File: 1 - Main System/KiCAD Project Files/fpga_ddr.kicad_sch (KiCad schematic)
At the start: 71 parts, among them IC8 IS43TR16640C-125JBL, IC9 IS43TR16640C-125JBL, U17 XC7Z020-1CLG484C

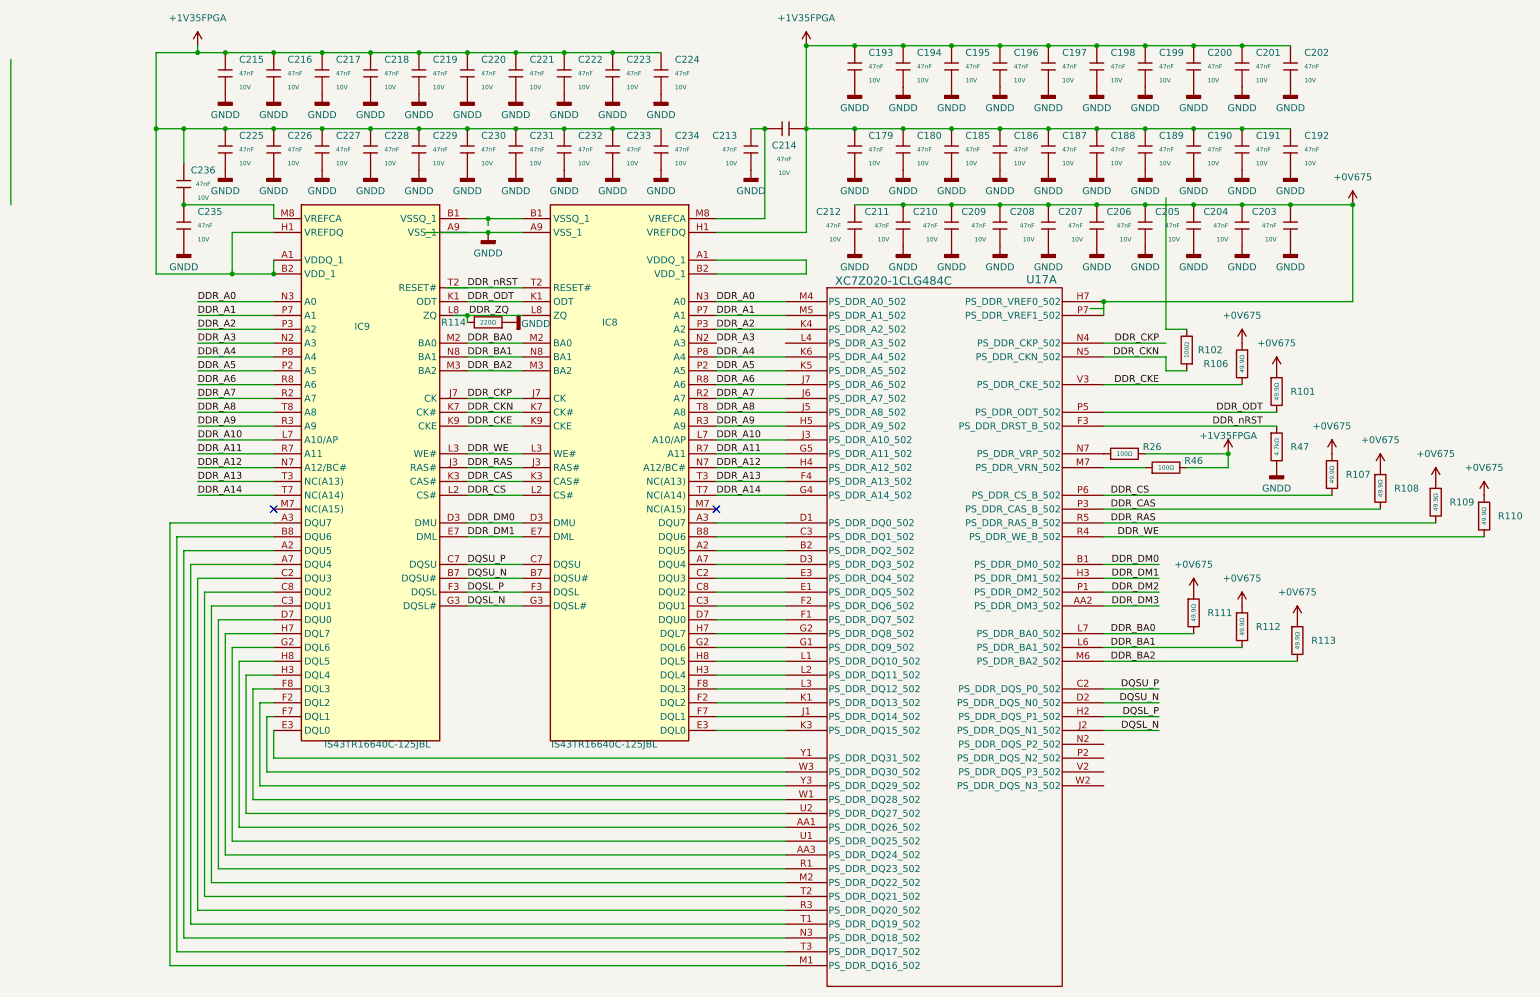
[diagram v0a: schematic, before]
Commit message: Routing DDR3 Completed (pre-review)
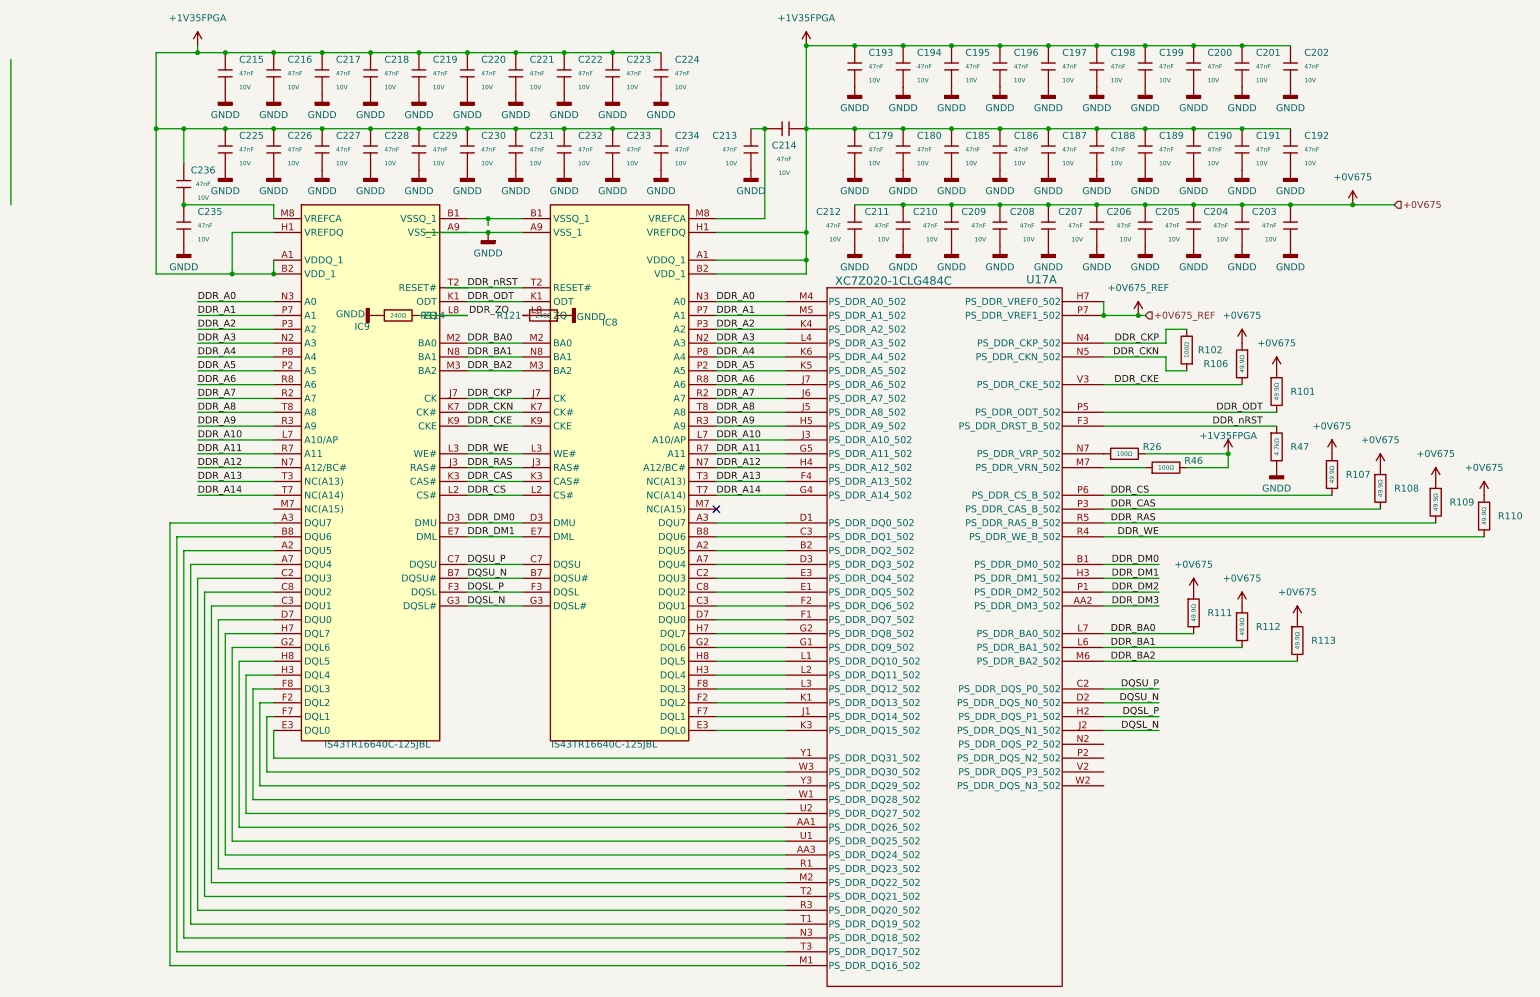
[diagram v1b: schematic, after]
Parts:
- added R121: 240Ω, PCM_JLCPCB:R_0402, symbol PCM_JLCPCB-Resistors:0402,220Ω
- R114: value 220Ω -> 240Ω
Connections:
- net +0V675: no longer U17.H7 (PS_DDR_VREF0_502), U17.P7 (PS_DDR_VREF1_502)
- net +1V35FPGA: now also IC8.A1 (VDDQ_1), IC8.A8 (VDDQ_2), IC8.B2 (VDD_1), IC8.C1 (VDDQ_3), IC8.C9 (VDDQ_4), IC8.D2 (VDDQ_5), IC8.D9 (VDD_2), IC8.E9 (VDDQ_6), IC8.F1 (VDDQ_7), IC8.G7 (VDD_3), IC8.H2 (VDDQ_8), IC8.H9 (VDDQ_9), IC8.K2 (VDD_4), IC8.K8 (VDD_5), IC8.N1 (VDD_6), IC8.N9 (VDD_7), IC8.R1 (VDD_8), IC8.R9 (VDD_9)
- net DDR_A3: now also U17.L4 (PS_DDR_A3_502)
- net DDR_CKP: now also R102.2
- net DDR_ZQ: no longer IC8.L8 (ZQ), IC9.L8 (ZQ), R114.2
- net GNDD: now also R121.1
- new net: IC8.L8 (ZQ), R121.2
- new net: IC9.L8 (ZQ), R114.2
- new net +0V675_REF: U17.H7 (PS_DDR_VREF0_502), U17.P7 (PS_DDR_VREF1_502)
- no-connect marks 2 -> 1
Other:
- moved on the sheet: R114
